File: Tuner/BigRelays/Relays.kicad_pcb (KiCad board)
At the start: 2 copper layers, 100 x 100 mm, 86 parts, among them J1 Conn_01x03, J10 Conn_01x02, J11 Conn_01x02, J12 Conn_01x01, J13 Conn_01x01, J14 Conn_01x01, J15 Conn_01x01, J16 Conn_01x02, J17 Conn_02x10_Odd_Even, J18 Conn_01x02, J19 Conn_01x03, J2 Conn_01x03, J3 Conn_01x03, J4 Conn_01x03, J5 Conn_01x03, J6 Conn_01x03, J7 Conn_01x03, J8 Conn_01x02, J9 Conn_01x02

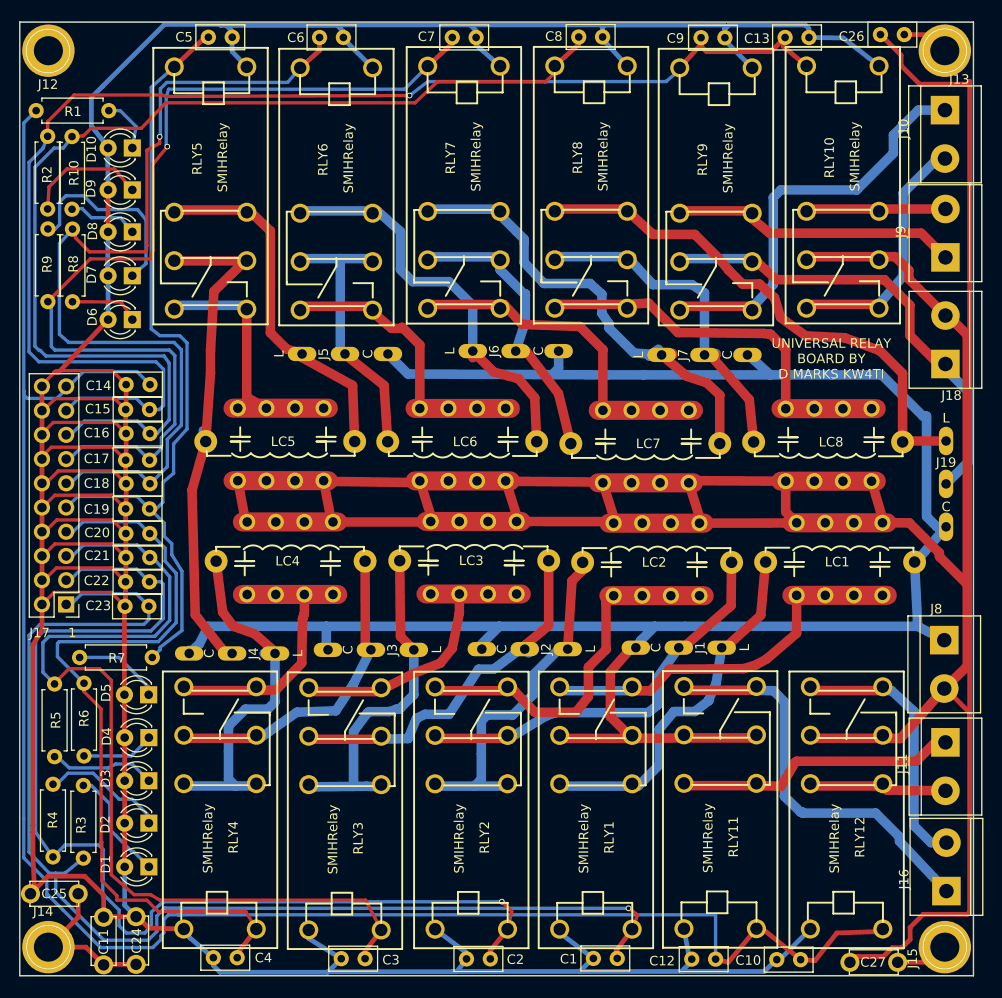
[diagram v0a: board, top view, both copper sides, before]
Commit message: Added HK19F boards
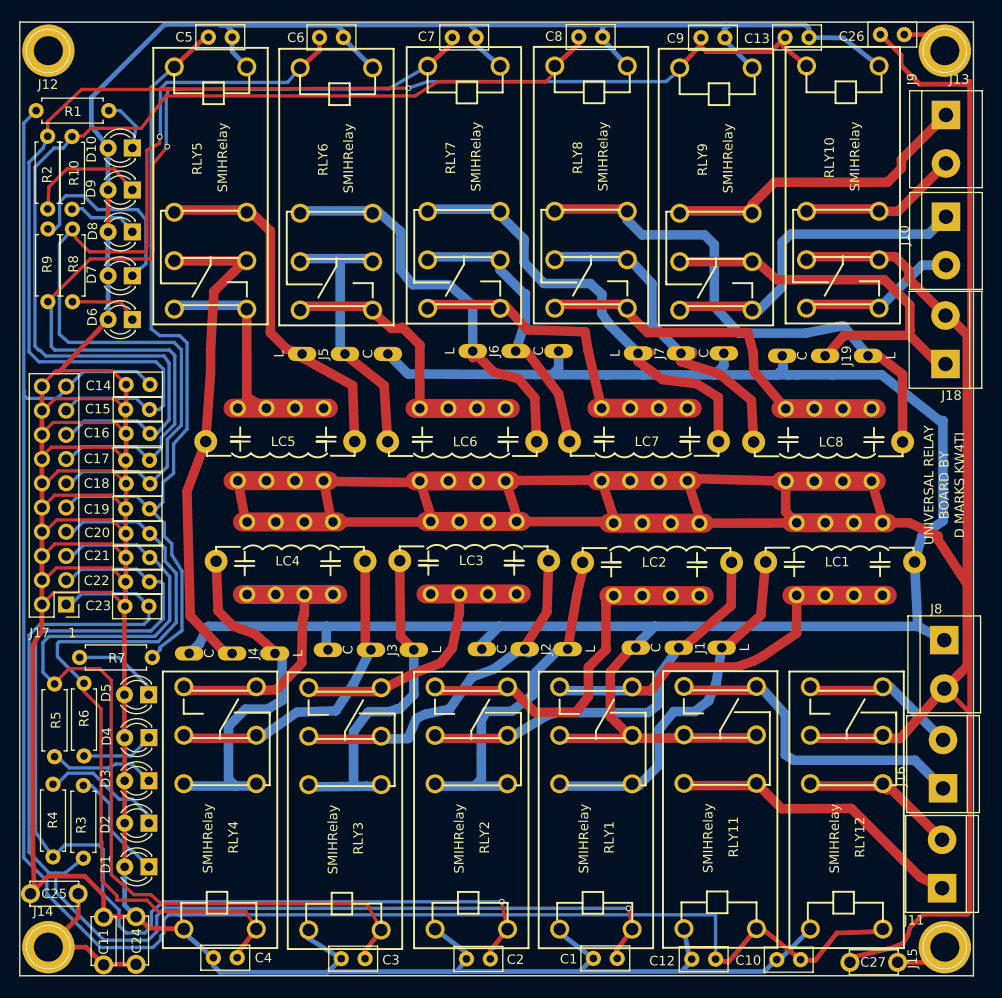
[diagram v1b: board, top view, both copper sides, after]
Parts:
- moved J19 18.5 mm to (134.4, 85.0), turned to 180 degrees
- moved J11 15.3 mm to (146.7, 140.8), turned to 90 degrees
- moved J9 14.9 mm to (147.1, 59.7), turned to 270 degrees
- moved J10 11.2 mm to (147.1, 70.4)
- moved J16 10.8 mm to (146.8, 130.4)
- moved J7 2.48 mm to (119.3, 84.7)
- moved LC7 0.26 mm to (115.3, 94.0)
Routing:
- net Net-(J16-Pad2): track 27.8 -> 16.2 mm
- net Net-(J10-Pad2): track 26.1 -> 16.5 mm
- net Net-(J16-Pad1): track 43.4 -> 35.1 mm
- net Net-(J10-Pad1): track 42.9 -> 34.8 mm
- net Net-(J18-Pad1): track 48.8 -> 44.6 mm
- net Net-(J9-Pad1): track 30.3 -> 34.1 mm
- net Net-(J11-Pad2): track 14.3 -> 16.9 mm
- net Net-(J7-Pad1): track 50.8 -> 48.5 mm
- net Net-(J9-Pad2): track 14.6 -> 16.7 mm
- net Net-(J4-Pad1): track 39.0 -> 40.7 mm
- net Net-(J11-Pad1): track 29.7 -> 31.4 mm
- net RFSIG: track 215.8 -> 217.4 mm
- net Net-(LC8-Pad1): track 32.5 -> 31.0 mm
- net Net-(J2-Pad2): track 39.2 -> 38.1 mm
- net RLY9: track 142.9 -> 143.7 mm
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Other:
- board text added: "Relays are SONGLE SMIH-SL-C SERIES HUI KE HK14FH/HK14FD TE CONNECTIVITY/SCHRACK RP/RTH SERIES"
- board text removed: "Relays are SONGLE SMIH-SL-C SERIES TE CONNECTIVITY/SCHRACK RP/RTH SERIES"

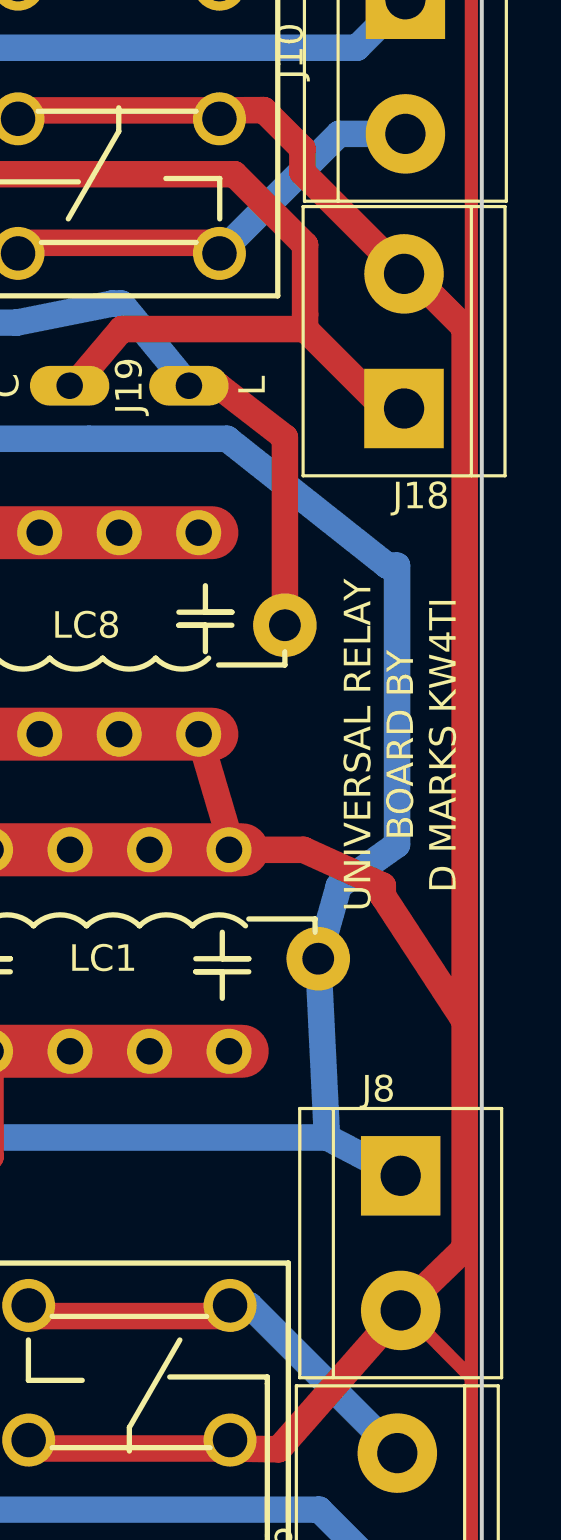
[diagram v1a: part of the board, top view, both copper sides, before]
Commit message: Error in pinout HK19F fixed
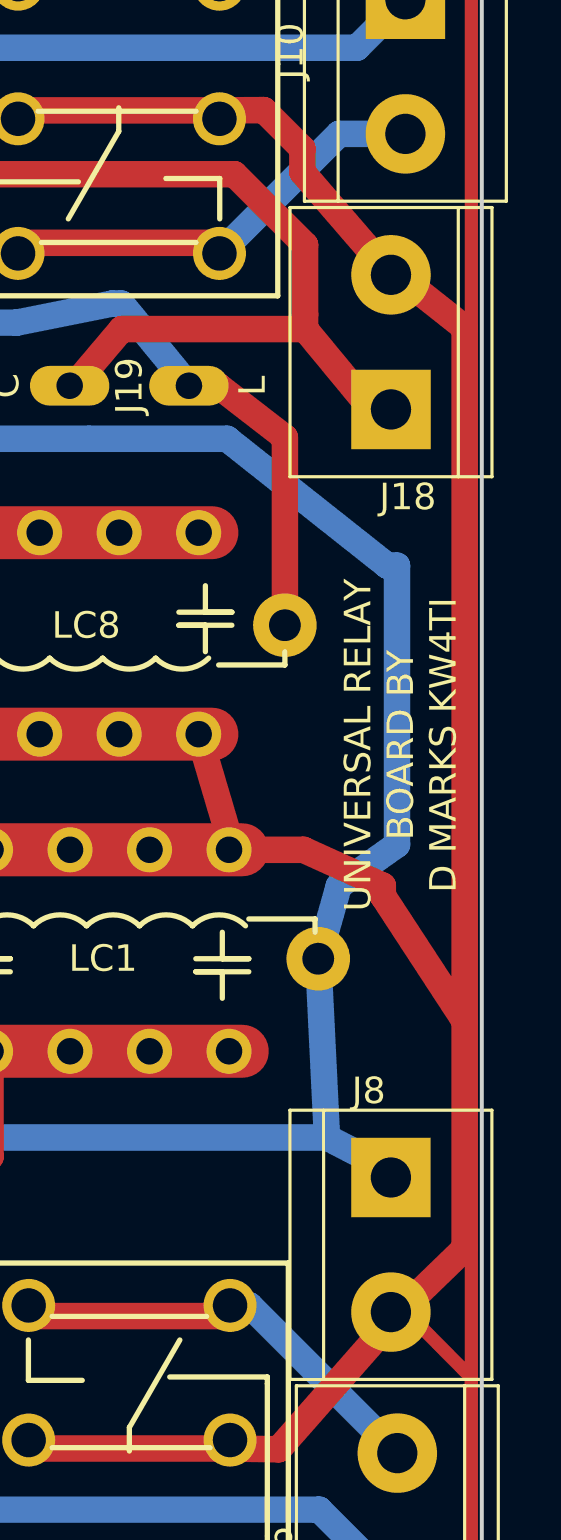
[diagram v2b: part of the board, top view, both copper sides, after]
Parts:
- moved J18 0.49 mm to (146.6, 85.9)
- moved J8 0.37 mm to (146.6, 114.9)
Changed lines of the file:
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@@
     (links 287)
     (no_connects 0)
-    (area 49.924999 49.924999 150.075001 150.075001)
+    (area 44.941618 47.773 153.221 151.075)
     (thickness 1.6)
     (drawings 25)
@@
   )
   (module Connectors_Terminal_Blocks:TerminalBlock_bornier-2_P5.08mm (layer F.Cu)
-    (at 146.939 114.808 270)
+    (at 146.5707 114.8715 270)
     (descr "simple 2-pin terminal block, pitch 5.08mm, revamped version of bornier2")
     (tags "terminal block bornier2")
@@
   )
   (module Connectors_Terminal_Blocks:TerminalBlock_bornier-2_P5.08mm (layer F.Cu)
-    (at 147.066 85.852 90)
+    (at 146.57324 85.88756 90)
     (descr "simple 2-pin terminal block, pitch 5.08mm, revamped version of bornier2")
     (tags "terminal block bornier2")
@@
     (effects (font (size 1 1) (thickness 0.15)) (justify mirror))
   )
-  (gr_text RF (at 144.272 115.2525 90) (layer B.SilkS)
+  (gr_text RF (at 143.9799 115.062 90) (layer B.SilkS)
     (effects (font (size 1 1) (thickness 0.15)) (justify mirror))
   )
@@
     (effects (font (size 1 1) (thickness 0.15)) (justify mirror))
   )
-  (gr_text GND (at 144.272 119.888 90) (layer B.SilkS)
+  (gr_text GND (at 144.018 119.9007 90) (layer B.SilkS)
     (effects (font (size 1 1) (thickness 0.15)) (justify mirror))
   )
@@
     (effects (font (size 1 1) (thickness 0.15)) (justify mirror))
   )
-  (gr_text RF (at 144.399 85.7885 90) (layer B.SilkS)
+  (gr_text RF (at 144.14246 85.80374 90) (layer B.SilkS)
     (effects (font (size 1 1) (thickness 0.15)) (justify mirror))
   )
@@
     (effects (font (size 1 1) (thickness 0.15)) (justify mirror))
   )
-  (gr_text GND (at 144.4625 80.8355 90) (layer B.SilkS)
+  (gr_text GND (at 143.83512 80.83042 90) (layer B.SilkS)
     (effects (font (size 1 1) (thickness 0.15)) (justify mirror))
   )
@@
   (segment (start 130.3152 98.1418) (end 130.3152 101.3592) (width 1) (layer F.Cu) (net 1))
   (segment (start 130.3152 101.3592) (end 131.4615 102.5055) (width 1) (layer F.Cu) (net 1))
-  (segment (start 147.066 80.772) (end 147.32 80.772) (width 1) (layer F.Cu) (net 1))
-  (segment (start 147.32 80.772) (end 149.352 82.804) (width 1) (layer F.Cu) (net 1))
+  (segment (start 146.57324 80.80756) (end 146.82724 80.80756) (width 1) (layer F.Cu) (net 1) (status 30))
+  (segment (start 146.82724 80.80756) (end 149.352 82.804) (width 1) (layer F.Cu) (net 1) (status 10))
   (segment (start 149.352 82.804) (end 149.352 108.966) (width 1) (layer F.Cu) (net 1))
   (segment (start 72.8604 98.091) (end 73.6478 102.2228) (width 1) (layer F.Cu) (net 1) (status 10))
@@
   (segment (start 149.3012 56.515) (end 144.3736 56.515) (width 0.5) (layer F.Cu) (net 1))
   (segment (start 149.606 56.2102) (end 149.3012 56.515) (width 0.5) (layer F.Cu) (net 1))
-  (segment (start 143.2306 76.9366) (end 147.066 80.772) (width 1) (layer F.Cu) (net 1))
+  (segment (start 143.2306 76.9366) (end 146.57324 80.80756) (width 1) (layer F.Cu) (net 1) (status 20))
   (segment (start 143.2306 76.0476) (end 143.2306 76.9366) (width 1) (layer F.Cu) (net 1))
   (segment (start 146.939 119.888) (end 147.0914 119.888) (width 0.5) (layer F.Cu) (net 1) (status 30))
@@
   (segment (start 136.4107 82.8548) (end 143.3322 82.8548) (width 1) (layer F.Cu) (net 52))
   (segment (start 126.8 75.12) (end 119.2 75.12) (width 1) (layer F.Cu) (net 52))
-  (segment (start 147.066 85.852) (end 147.066 86.36) (width 1) (layer B.Cu) (net 52))
+  (segment (start 146.57324 85.88756) (end 146.57324 86.39556) (width 1) (layer B.Cu) (net 52) (status 30))
   (segment (start 126.8 74.8) (end 126.8786 74.8) (width 1) (layer F.Cu) (net 52) (status 30))
   (segment (start 126.8786 74.8) (end 129.3876 77.0128) (width 1) (layer F.Cu) (net 52) (status 10))
-  (segment (start 143.3322 82.8548) (end 146.3294 85.852) (width 1) (layer F.Cu) (net 52))
+  (segment (start 143.3322 82.8548) (end 145.83664 85.88756) (width 1) (layer F.Cu) (net 52) (status 20))
   (segment (start 143.3322 79.6798) (end 143.3322 82.3087) (width 1) (layer F.Cu) (net 52))
   (segment (start 143.3322 82.3087) (end 143.3322 82.8548) (width 1) (layer F.Cu) (net 52))
   (segment (start 140.6652 77.0128) (end 143.3322 79.6798) (width 1) (layer F.Cu) (net 52))
   (segment (start 129.3876 77.0128) (end 140.6652 77.0128) (width 1) (layer F.Cu) (net 52))
-  (segment (start 146.3294 85.852) (end 147.066 85.852) (width 1) (layer F.Cu) (net 52))
+  (segment (start 145.83664 85.88756) (end 146.57324 85.88756) (width 1) (layer F.Cu) (net 52) (status 30))
   (segment (start 113.7 70.7613) (end 115.2525 72.3138) (width 1) (layer B.Cu) (net 53))
   (segment (start 136.40308 81.89214) (end 138.94728 84.99348) (width 1) (layer B.Cu) (net 53) (status 20))

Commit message: JLCPCB Nov 1 2018
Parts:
- removed C26: 10 nF, Capacitors_THT:C_Disc_D5.0mm_W2.5mm_P2.50mm
- removed C27: 10 nF, Capacitors_THT:C_Disc_D5.0mm_W2.5mm_P5.00mm
- added J21: Conn_01x01, tuner:SOLDERJUMPER, F.Cu at (128.9, 118.7)
- added J22: Conn_01x01, tuner:SOLDERJUMPER, F.Cu at (128.9, 129.3)
- added J23: Conn_01x01, tuner:SOLDERJUMPER, F.Cu at (142.4, 116.7)
- added J24: Conn_01x01, tuner:SOLDERJUMPER, F.Cu at (128.4, 70.1)
- added J25: Conn_01x01, tuner:SOLDERJUMPER, F.Cu at (129.7, 81.4)
- added J27: Conn_01x01, tuner:SOLDERJUMPER, F.Cu at (142.3, 148.4)
- added J28: Conn_01x01, tuner:SOLDERJUMPER, F.Cu at (138.9, 148.6)
- added J29: Conn_01x01, tuner:SOLDERJUMPER, F.Cu at (141.7, 51.2)
- added J30: Conn_01x01, tuner:SOLDERJUMPER, F.Cu at (138.4, 51.3)
- moved C9 2.95 mm to (118.5, 51.7)
- moved C13 1.52 mm to (131.8, 51.6)
- moved RLY10 0.17 mm to (136.3, 64.8)
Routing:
- net RFGND: track 322.1 -> 210.8 mm
- net Net-(J15-Pad1): track 5.92 -> 12.7 mm
- net Net-(J13-Pad1): track 6.43 -> 11.2 mm
- net Net-(J16-Pad2): track 16.2 -> 19.4 mm
- net Net-(J11-Pad2): track 16.9 -> 19.8 mm
- net Net-(J10-Pad2): track 16.5 -> 19.4 mm
- net Net-(J24-Pad1): track 16.7 -> 19.6 mm
- net RLY9: track 143.7 -> 146.3 mm
- net +5V: track 478.9 -> 481.5 mm
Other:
- board text added: "NC GND"
- board text added: "NO GND"
- board text added: "Relays are SONGLE SMIH-SL-C SERIES HUI KE HK14FH/HK14FD TE CONNECTIVITY/SCHRACK RP/RTH SERIES OMRON G2RL-1 PANASONIC JW 2 FORM C"
- board text removed: "Relays are SONGLE SMIH-SL-C SERIES HUI KE HK14FH/HK14FD TE CONNECTIVITY/SCHRACK RP/RTH SERIES"

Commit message: First code commit
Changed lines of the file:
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@@
     (links 292)
     (no_connects 0)
-    (area 49.924999 49.924999 150.075001 150.075001)
+    (area 44.941618 46.95878 152.967 152.888419)
     (thickness 1.6)
     (drawings 30)
-    (tracks 1023)
+    (tracks 1025)
     (zones 0)
     (modules 93)
@@
   )
   (setup
-    (last_trace_width 0.35)
+    (last_trace_width 1)
     (user_trace_width 0.35)
     (user_trace_width 0.5)
@@
   (segment (start 100.8012 79.6176) (end 103.251 82.2674) (width 1) (layer F.Cu) (net 21))
   (segment (start 103.251 82.2674) (end 109.277785 82.477785) (width 1) (layer F.Cu) (net 21))
-  (segment (start 126.8 80.2) (end 127.5212 79.2094) (width 1) (layer B.Cu) (net 22))
-  (segment (start 127.5212 79.2094) (end 129.9464 76.7842) (width 1) (layer B.Cu) (net 22))
-  (segment (start 129.9464 76.7842) (end 129.9464 73.1012) (width 0.35) (layer B.Cu) (net 22))
-  (segment (start 129.9464 73.1012) (end 130.81 72.2376) (width 1) (layer B.Cu) (net 22))
-  (segment (start 130.81 72.2376) (end 145.288 72.2376) (width 1) (layer B.Cu) (net 22))
+  (segment (start 129.86766 76.86294) (end 129.86766 73.17994) (width 1) (layer B.Cu) (net 22))
   (segment (start 145.288 72.2376) (end 147.1168 70.4088) (width 1) (layer B.Cu) (net 22))
+  (segment (start 130.81 72.2376) (end 145.288 72.2376) (width 1) (layer B.Cu) (net 22))
+  (segment (start 129.9464 73.1012) (end 130.81 72.2376) (width 1) (layer B.Cu) (net 22))
+  (segment (start 129.86766 73.17994) (end 129.9464 73.1012) (width 1) (layer B.Cu) (net 22))
+  (segment (start 126.8 80.2) (end 127.5212 79.2094) (width 1) (layer B.Cu) (net 22))
+  (segment (start 127.5212 79.2094) (end 129.86766 76.86294) (width 1) (layer B.Cu) (net 22))
+  (segment (start 129.86766 76.86294) (end 129.9464 76.7842) (width 1) (layer B.Cu) (net 22))
   (segment (start 126.8 79.8) (end 119.2 79.8) (width 1) (layer F.Cu) (net 22) (status 30))
   (segment (start 126.8 79.8) (end 126.923 79.8) (width 1) (layer B.Cu) (net 22) (status 30))

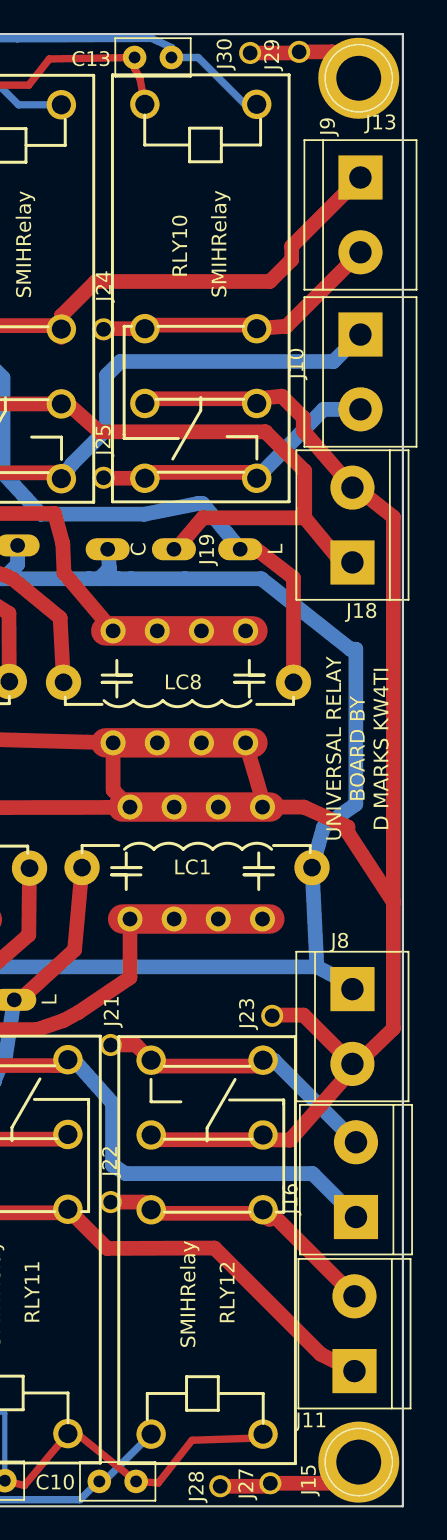
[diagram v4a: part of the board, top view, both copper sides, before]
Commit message: Moved some grounds around
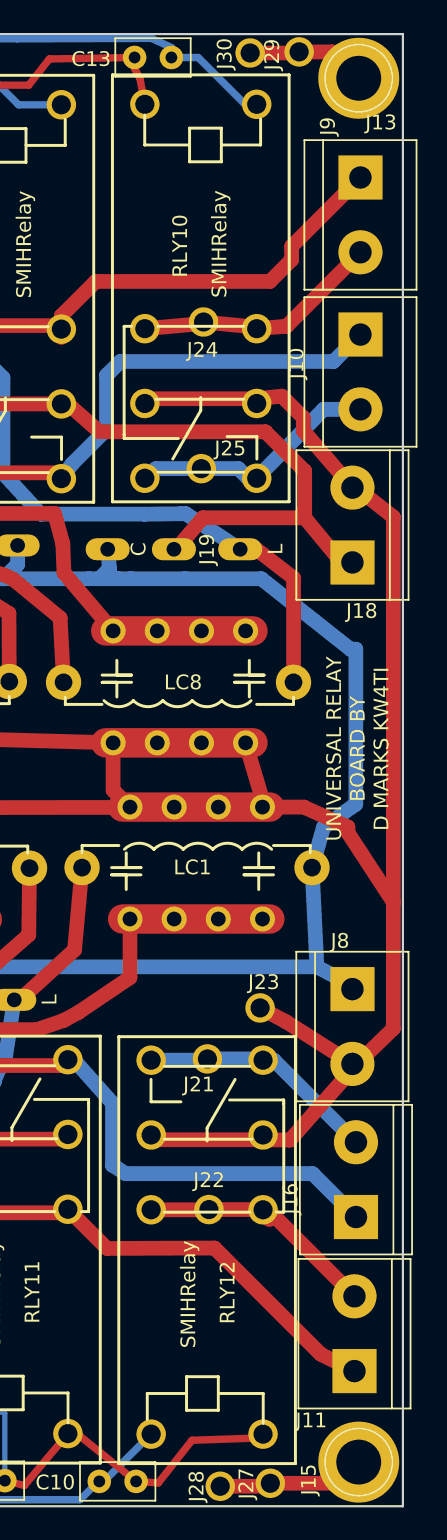
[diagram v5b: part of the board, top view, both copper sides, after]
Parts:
- moved J24 6.81 mm to (135.2, 69.6)
- moved J22 6.69 mm to (135.6, 129.8)
- moved J25 6.67 mm to (136.3, 80.8)
- moved J21 6.64 mm to (135.5, 119.6)
- moved J23 0.98 mm to (141.6, 116.1)
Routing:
- net Net-(J16-Pad2): track 19.4 -> 16.3 mm
- net Net-(J11-Pad2): track 19.8 -> 16.9 mm
- net Net-(J24-Pad1): track 19.6 -> 16.9 mm
- net Net-(J10-Pad2): track 19.4 -> 17.2 mm
- net Net-(J19-Pad1): track 55.8 -> 55.0 mm
- net RFGND: track 210.8 -> 211.4 mm

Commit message: JLCPCB order 2019-03-25
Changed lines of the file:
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@@
     (links 292)
     (no_connects 0)
-    (area 49.924999 49.924999 150.075001 150.075001)
+    (area 44.941618 46.95878 152.967 152.888419)
     (thickness 1.6)
     (drawings 30)
@@
   )
   (setup
-    (last_trace_width 1)
+    (last_trace_width 0.25)
     (user_trace_width 0.35)
     (user_trace_width 0.5)
@@
     (descr "simple 2-pin terminal block, pitch 5.08mm, revamped version of bornier2")
     (tags "terminal block bornier2")
-    (fp_text reference J16 (at 1.2474 -4.4426 90) (layer F.SilkS)
-      (effects (font (size 1 1) (thickness 0.15)))
-    )
+    (fp_text reference J16 (at 3.0988 2.3495 90) (layer F.SilkS)
+      (effects (font (size 1 1) (thickness 0.15)))
+    )
